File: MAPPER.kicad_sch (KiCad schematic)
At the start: 26 parts, among them U14 74AHC139, U15 74LVC1G04, U17 74LVC1G04, U19 74HC245, U21 74LVC1G02, U22 74AHC273, U23 74HC245, U24 74LVC1G02, U25 74AHC273, U26 74HC245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

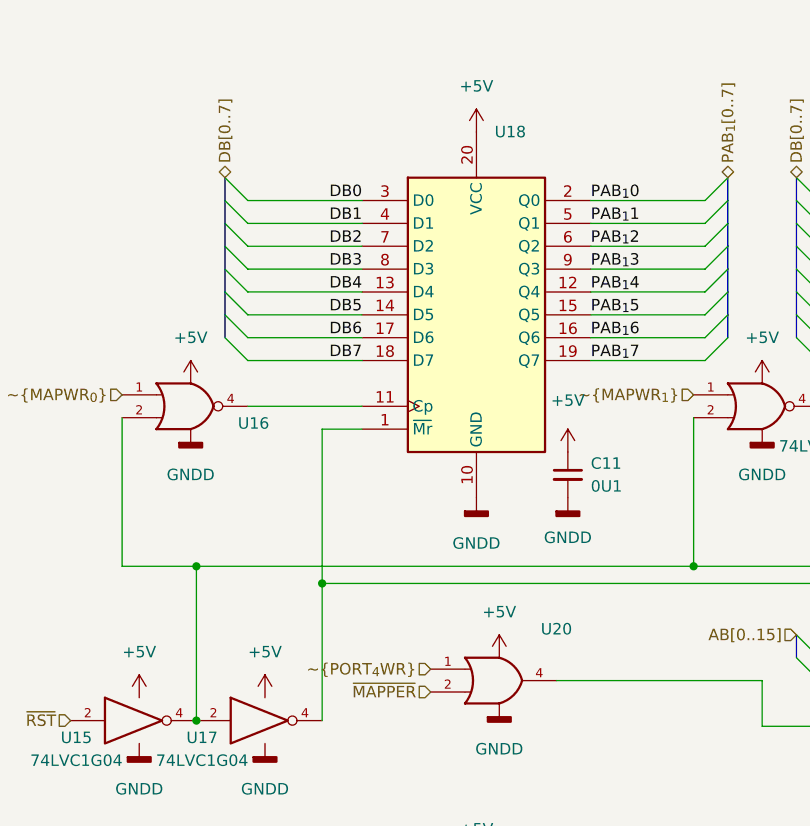
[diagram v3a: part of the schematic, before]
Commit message: begin integration of logic into atf1508
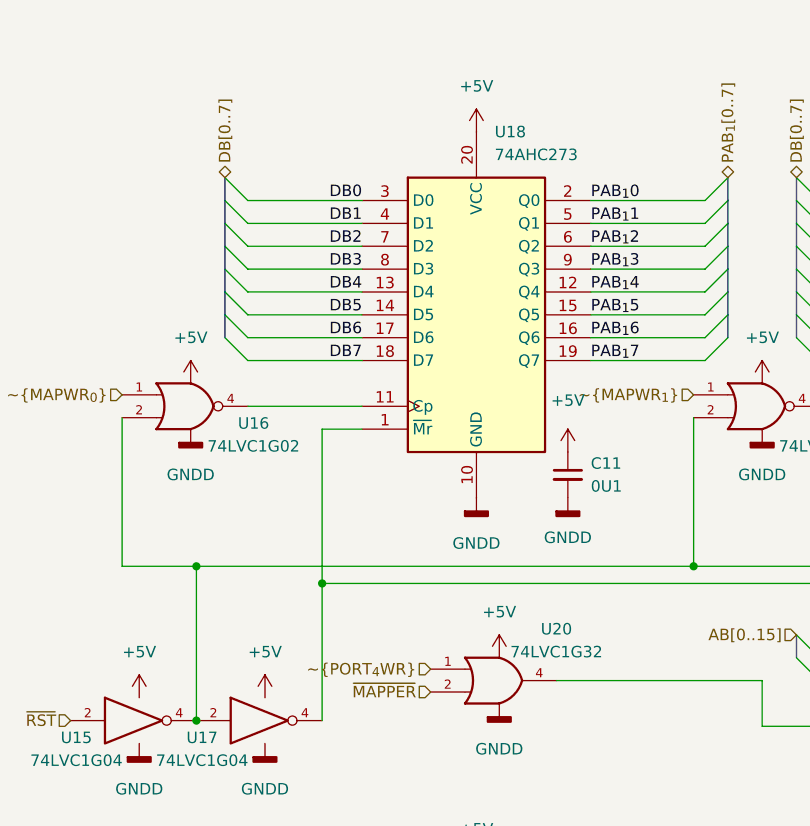
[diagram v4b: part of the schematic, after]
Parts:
- C10, C11, C12, C13, C14, C15, C16, C17, C18: footprint (none) -> Capacitor_SMD:C_0603_1608Metric
- U14: footprint (none) -> Package_SO:TSSOP-16_4.4x5mm_P0.65mm
- U15, U17, U21, U24, U27, U28: footprint (none) -> Package_TO_SOT_SMD:SOT-353_SC-70-5
- U16: value (none) -> 74LVC1G02; footprint (none) -> Package_TO_SOT_SMD:SOT-353_SC-70-5
- U18: value (none) -> 74AHC273; footprint (none) -> Package_SO:TSSOP-20_4.4x6.5mm_P0.65mm
- U19, U22, U23, U25, U26, U29, U30: footprint (none) -> Package_SO:TSSOP-20_4.4x6.5mm_P0.65mm
- U20: value (none) -> 74LVC1G32; footprint (none) -> Package_TO_SOT_SMD:SOT-353_SC-70-5
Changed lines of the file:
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@@
       (effects (font (size 1.27 1.27)) (justify left))
     )
-    (property "Footprint" "" (id 2) (at 73.66 151.13 0)
+    (property "Footprint" "Capacitor_SMD:C_0603_1608Metric" (id 2) (at 73.66 151.13 0)
       (effects (font (size 1.27 1.27)) hide)
     )
@@
     (property "Reference" "U21" (id 0) (at 102.235 62.865 0))
     (property "Value" "74LVC1G02" (id 1) (at 102.235 65.405 0))
-    (property "Footprint" "" (id 2) (at 95.25 60.96 0)
+    (property "Footprint" "Package_TO_SOT_SMD:SOT-353_SC-70-5" (id 2) (at 95.25 60.96 0)
       (effects (font (size 1.27 1.27)) hide)
     )
@@
       (effects (font (size 1.27 1.27)) (justify left))
     )
-    (property "Footprint" "" (id 2) (at 264.16 151.13 0)
+    (property "Footprint" "Capacitor_SMD:C_0603_1608Metric" (id 2) (at 264.16 151.13 0)
       (effects (font (size 1.27 1.27)) hide)
     )
@@
       (effects (font (size 1.27 1.27)) (justify left))
     )
-    (property "Footprint" "" (id 2) (at 29.21 187.96 0)
+    (property "Footprint" "Capacitor_SMD:C_0603_1608Metric" (id 2) (at 29.21 187.96 0)
       (effects (font (size 1.27 1.27)) hide)
     )
@@
     (property "Reference" "U14" (id 0) (at 254 81.28 0))
     (property "Value" "74AHC139" (id 1) (at 254 83.82 0))
-    (property "Footprint" "" (id 2) (at 254 91.44 0)
+    (property "Footprint" "Package_SO:TSSOP-16_4.4x5mm_P0.65mm" (id 2) (at 254 91.44 0)
       (effects (font (size 1.27 1.27)) hide)
     )
@@
       (effects (font (size 1.27 1.27)) (justify left))
     )
-    (property "Footprint" "" (id 2) (at 137.16 151.13 0)
+    (property "Footprint" "Capacitor_SMD:C_0603_1608Metric" (id 2) (at 137.16 151.13 0)
       (effects (font (size 1.27 1.27)) hide)
     )
@@
     (property "Reference" "U24" (id 0) (at 165.735 62.865 0))
     (property "Value" "74LVC1G02" (id 1) (at 165.735 65.405 0))
-    (property "Footprint" "" (id 2) (at 158.75 60.96 0)
+    (property "Footprint" "Package_TO_SOT_SMD:SOT-353_SC-70-5" (id 2) (at 158.75 60.96 0)
       (effects (font (size 1.27 1.27)) hide)
     )
@@
       (effects (font (size 1.27 1.27)) (justify left))
     )
-    (property "Footprint" "" (id 2) (at 73.66 68.58 0)
+    (property "Footprint" "Capacitor_SMD:C_0603_1608Metric" (id 2) (at 73.66 68.58 0)
       (effects (font (size 1.27 1.27)) hide)
     )
@@
     (property "Reference" "U27" (id 0) (at 199.39 85.725 0))
     (property "Value" "74LVC1G32" (id 1) (at 199.39 88.265 0))
-    (property "Footprint" "" (id 2) (at 193.04 91.44 0)
+    (property "Footprint" "Package_TO_SOT_SMD:SOT-353_SC-70-5" (id 2) (at 193.04 91.44 0)
       (effects (font (size 1.27 1.27)) hide)
     )
@@
       (effects (font (size 1.27 1.27)) (justify left))
     )
-    (property "Value" "" (id 1) (at 65.5194 33.02 0)
-      (effects (font (size 1.27 1.27)) (justify left))
-    )
-    (property "Footprint" "" (id 2) (at 63.5 50.8 0)
+    (property "Value" "74AHC273" (id 1) (at 65.5194 33.02 0)
+      (effects (font (size 1.27 1.27)) (justify left))
+    )
+    (property "Footprint" "Package_SO:TSSOP-20_4.4x6.5mm_P0.65mm" (id 2) (at 63.5 50.8 0)
       (effects (font (size 1.27 1.27)) hide)
     )
@@
       (effects (font (size 1.27 1.27)) (justify left))
     )
-    (property "Footprint" "" (id 2) (at 21.59 177.165 0)
+    (property "Footprint" "Package_SO:TSSOP-16_4.4x5mm_P0.65mm" (id 2) (at 21.59 177.165 0)
       (effects (font (size 1.27 1.27)) hide)
     )
@@
       (effects (font (size 1.27 1.27)) (justify left))
     )
-    (property "Footprint" "" (id 2) (at 264.16 68.58 0)
+    (property "Footprint" "Capacitor_SMD:C_0603_1608Metric" (id 2) (at 264.16 68.58 0)
       (effects (font (size 1.27 1.27)) hide)
     )
@@
       (effects (font (size 1.27 1.27)) (justify left))
     )
-    (property "Footprint" "" (id 2) (at 127 133.35 0)
+    (property "Footprint" "Package_SO:TSSOP-20_4.4x6.5mm_P0.65mm" (id 2) (at 127 133.35 0)
       (effects (font (size 1.27 1.27)) hide)
     )
@@
       (effects (font (size 1.27 1.27)) (justify left))
     )
-    (property "Footprint" "" (id 2) (at 190.5 50.8 0)
+    (property "Footprint" "Package_SO:TSSOP-20_4.4x6.5mm_P0.65mm" (id 2) (at 190.5 50.8 0)
       (effects (font (size 1.27 1.27)) hide)
     )
@@
       (effects (font (size 1.27 1.27)) (justify left))
     )
-    (property "Footprint" "" (id 2) (at 200.66 151.13 0)
+    (property "Footprint" "Capacitor_SMD:C_0603_1608Metric" (id 2) (at 200.66 151.13 0)
       (effects (font (size 1.27 1.27)) hide)
     )
@@
     (property "Reference" "U14" (id 0) (at 127 101.6 0))
     (property "Value" "74AHC139" (id 1) (at 127 104.14 0))
-    (property "Footprint" "" (id 2) (at 127 91.44 0)
+    (property "Footprint" "Package_SO:TSSOP-16_4.4x5mm_P0.65mm" (id 2) (at 127 91.44 0)
       (effects (font (size 1.27 1.27)) hide)
     )
@@
       (effects (font (size 1.27 1.27)) (justify left))
     )
-    (property "Footprint" "" (id 2) (at 200.66 68.58 0)
+    (property "Footprint" "Capacitor_SMD:C_0603_1608Metric" (id 2) (at 200.66 68.58 0)
       (effects (font (size 1.27 1.27)) hide)
     )
@@
     (in_bom yes) (on_board yes)
     (property "Reference" "U20" (id 0) (at 72.39 85.725 0))
-    (property "Value" "" (id 1) (at 72.39 88.265 0))
-    (property "Footprint" "" (id 2) (at 66.04 91.44 0)
+    (property "Value" "74LVC1G32" (id 1) (at 72.39 88.265 0))
+    (property "Footprint" "Package_TO_SOT_SMD:SOT-353_SC-70-5" (id 2) (at 66.04 91.44 0)
       (effects (font (size 1.27 1.27)) hide)
     )
@@
       (effects (font (size 1.27 1.27)) (justify left))
     )
-    (property "Footprint" "" (id 2) (at 127 50.8 0)
+    (property "Footprint" "Package_SO:TSSOP-20_4.4x6.5mm_P0.65mm" (id 2) (at 127 50.8 0)
       (effects (font (size 1.27 1.27)) hide)
     )
@@
       (effects (font (size 1.27 1.27)) (justify left))
     )
-    (property "Footprint" "" (id 2) (at 63.5 133.35 0)
+    (property "Footprint" "Package_SO:TSSOP-20_4.4x6.5mm_P0.65mm" (id 2) (at 63.5 133.35 0)
       (effects (font (size 1.27 1.27)) hide)
     )
@@
       (effects (font (size 1.27 1.27)) (justify left))
     )
-    (property "Footprint" "" (id 2) (at 254 50.8 0)
+    (property "Footprint" "Package_SO:TSSOP-20_4.4x6.5mm_P0.65mm" (id 2) (at 254 50.8 0)
       (effects (font (size 1.27 1.27)) hide)
     )
@@
       (effects (font (size 1.27 1.27)) (justify left))
     )
-    (property "Footprint" "" (id 2) (at 190.5 133.35 0)
+    (property "Footprint" "Package_SO:TSSOP-20_4.4x6.5mm_P0.65mm" (id 2) (at 190.5 133.35 0)
       (effects (font (size 1.27 1.27)) hide)
     )
@@
       (effects (font (size 1.27 1.27)) (justify left))
     )
-    (property "Footprint" "" (id 2) (at 254 133.35 0)
+    (property "Footprint" "Package_SO:TSSOP-20_4.4x6.5mm_P0.65mm" (id 2) (at 254 133.35 0)
       (effects (font (size 1.27 1.27)) hide)
     )
@@
     (property "Reference" "U17" (id 0) (at 33.02 97.79 0))
     (property "Value" "74LVC1G04" (id 1) (at 33.02 100.33 0))
-    (property "Footprint" "" (id 2) (at 40.005 95.885 0)
+    (property "Footprint" "Package_TO_SOT_SMD:SOT-353_SC-70-5" (id 2) (at 40.005 95.885 0)
       (effects (font (size 1.27 1.27)) hide)
     )
@@
     (property "Reference" "U15" (id 0) (at 19.05 97.79 0))
     (property "Value" "74LVC1G04" (id 1) (at 19.05 100.33 0))
-    (property "Footprint" "" (id 2) (at 26.035 95.885 0)
+    (property "Footprint" "Package_TO_SOT_SMD:SOT-353_SC-70-5" (id 2) (at 26.035 95.885 0)
       (effects (font (size 1.27 1.27)) hide)
     )
@@
     (in_bom yes) (on_board yes)
     (property "Reference" "U16" (id 0) (at 38.735 62.865 0))
-    (property "Value" "" (id 1) (at 38.735 65.405 0))
-    (property "Footprint" "" (id 2) (at 31.75 60.96 0)
+    (property "Value" "74LVC1G02" (id 1) (at 38.735 65.405 0))
+    (property "Footprint" "Package_TO_SOT_SMD:SOT-353_SC-70-5" (id 2) (at 31.75 60.96 0)
       (effects (font (size 1.27 1.27)) hide)
     )
@@
       (effects (font (size 1.27 1.27)) (justify left))
     )
-    (property "Footprint" "" (id 2) (at 137.16 68.58 0)
+    (property "Footprint" "Capacitor_SMD:C_0603_1608Metric" (id 2) (at 137.16 68.58 0)
       (effects (font (size 1.27 1.27)) hide)
     )
@@
     (property "Reference" "U28" (id 0) (at 229.235 62.865 0))
     (property "Value" "74LVC1G02" (id 1) (at 229.235 65.405 0))
-    (property "Footprint" "" (id 2) (at 222.25 60.96 0)
-      (effects (font (size 1.27 1.27)) hide)
-    )
+    (property "Footprint" "Package_TO_SOT_SMD:SOT-353_SC-70-5" (id 2) (at 222.25 60.96 0)
+      (effects (font (size 1.27 1.27)) hide)
+    )
